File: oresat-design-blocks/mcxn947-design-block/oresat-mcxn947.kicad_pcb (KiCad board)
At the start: 2 copper layers, 1 part, among them IC1 MCXN947VKLT

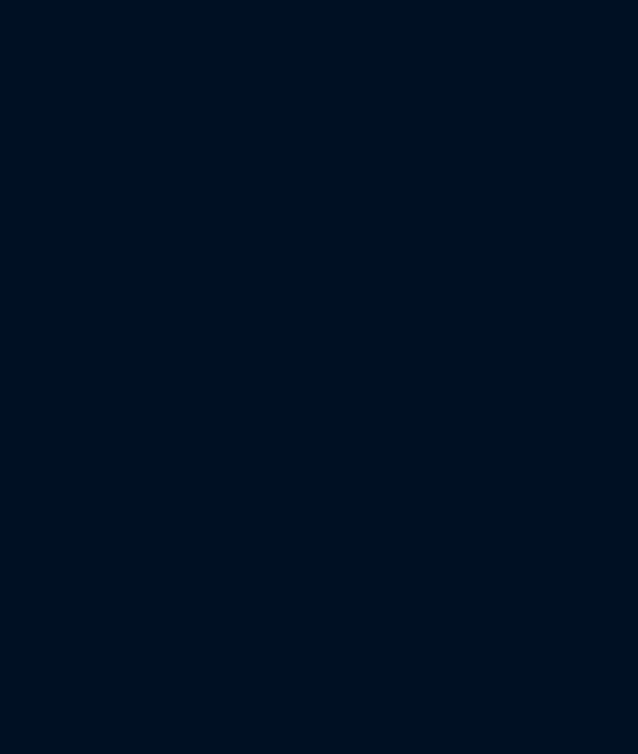
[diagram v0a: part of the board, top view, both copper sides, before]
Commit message: Removed lock file, updated .gitignore file
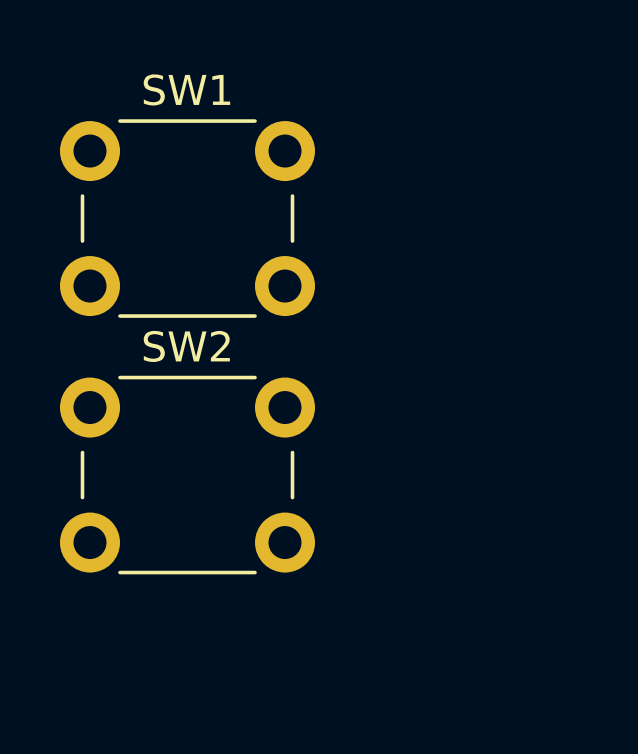
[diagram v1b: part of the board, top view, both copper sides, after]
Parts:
- added SW1: RESET, Button_Switch_THT:SW_PUSH_6mm, F.Cu at (19.9, 21.2)
- added SW2: ISP(BOOT), Button_Switch_THT:SW_PUSH_6mm, F.Cu at (19.9, 29.8)
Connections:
- IC1 pad 10: unconnected-(IC1C-P1_30-Pad10) -> Net-(IC1C-P1_30)
- IC1 pad 101: unconnected-(IC1A-EP-Pad101) -> GND
- IC1 pad 11: unconnected-(IC1C-P1_31-Pad11) -> Net-(IC1C-P1_31)
- IC1 pad 76: unconnected-(IC1B-P0_0-Pad76) -> Net-(IC1B-P0_0)
- IC1 pad 77: unconnected-(IC1B-P0_1-Pad77) -> Net-(IC1B-P0_1)
- IC1 pad 78: unconnected-(IC1B-P0_2-Pad78) -> Net-(IC1B-P0_2)
- IC1 pad 79: unconnected-(IC1B-P0_3-Pad79) -> Net-(IC1B-P0_3)
- IC1 pad 82: unconnected-(IC1B-P0_6-Pad82) -> Net-(IC1B-P0_6)
- IC1 pad 9: unconnected-(IC1A-RESET_B-Pad9) -> RESET

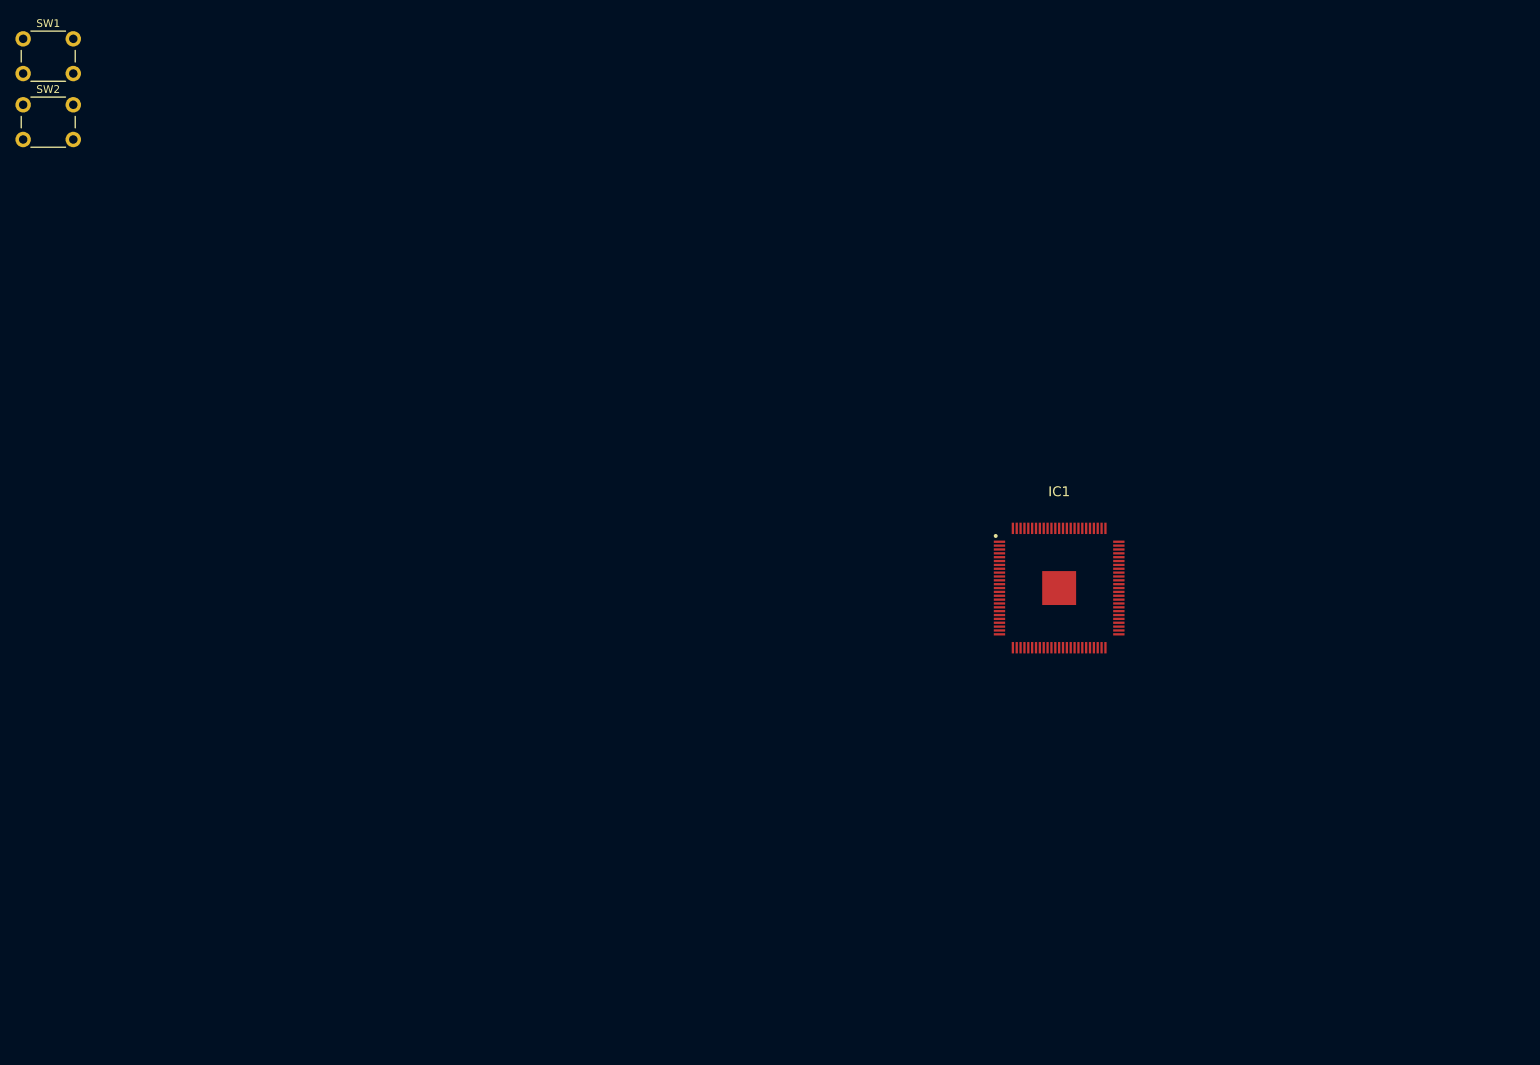
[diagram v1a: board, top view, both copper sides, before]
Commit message: Rough draft of schematic done. Power checked against eval board and reference manual. Needs one more go-over we think. Polished symbol, pin names might need another go-around with alt numbers. Added OreSat debug connector because that makes sense. Started 4 layer board layout, initial placements.
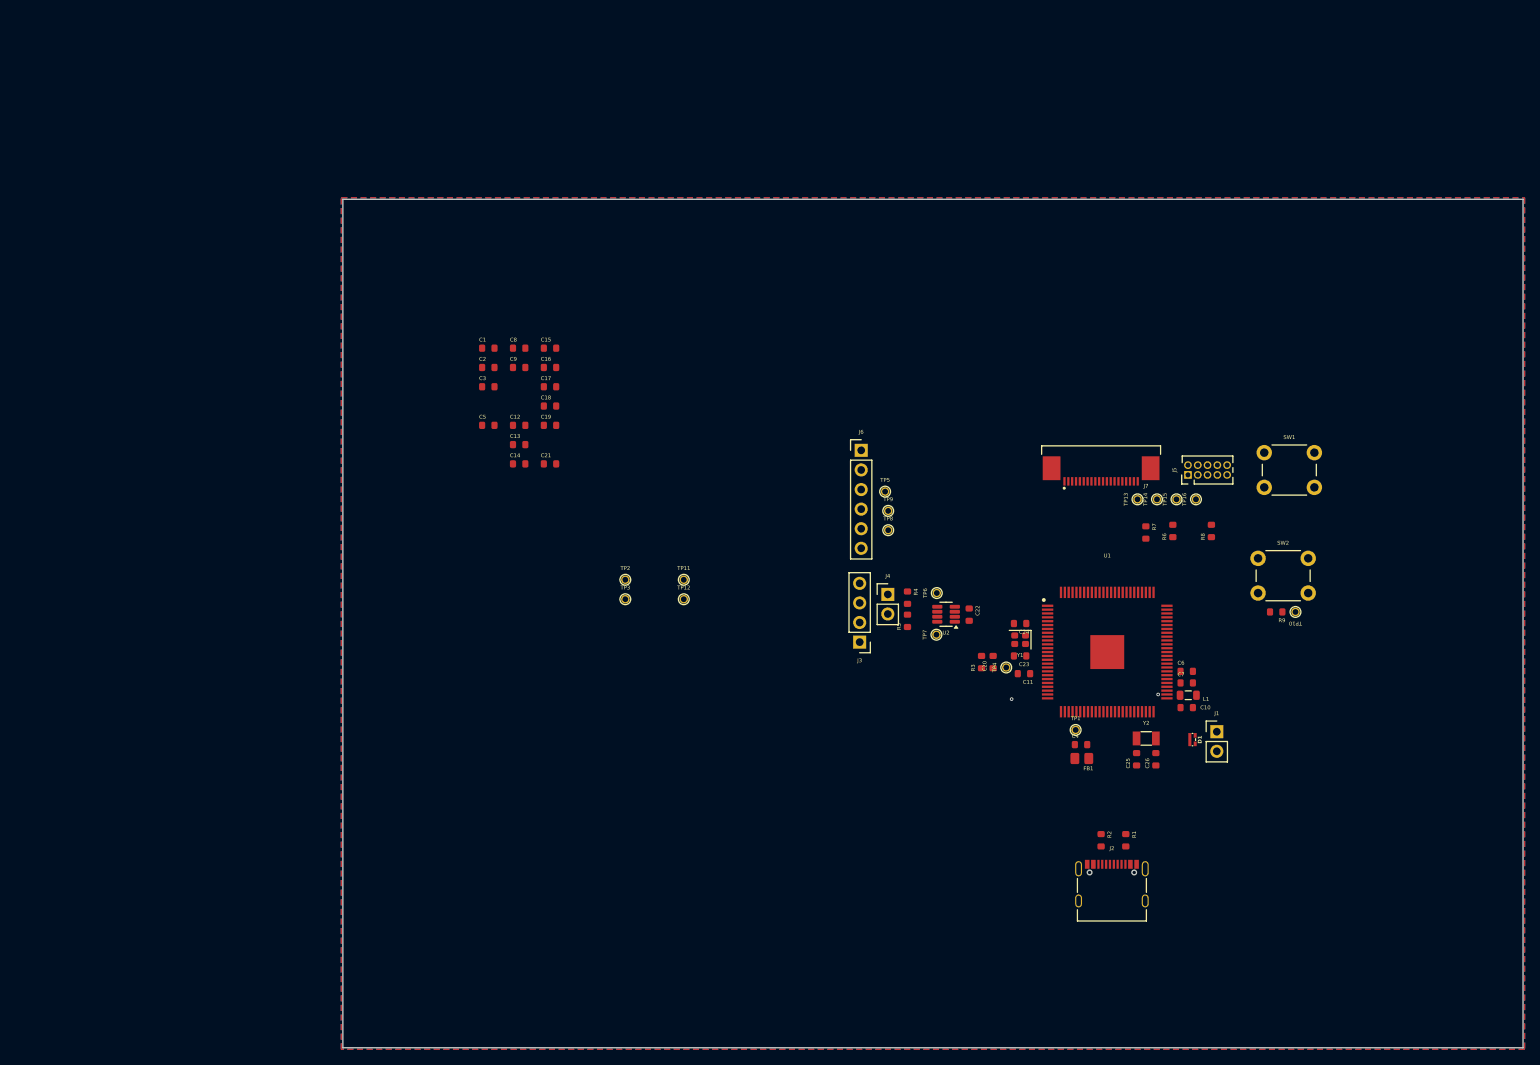
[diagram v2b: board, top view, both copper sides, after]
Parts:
- removed IC1: MCXN947VKLT, oresat-ics:MCXN947KVLT-QFP50P1600X1600X160-101N
- added C1: 100n, oresat-passives:0603-B-NOSILK, F.Cu at (80.3, 61.3)
- added C10: 6.8u, oresat-passives:0603-B-NOSILK, F.Cu at (170.8, 107.9)
- added C11: 4.7u, oresat-passives:0603-B-NOSILK, F.Cu at (149.7, 103.5)
- added C12: 100n, oresat-passives:0603-B-NOSILK, F.Cu at (84.3, 71.3)
- added C13: 100n, oresat-passives:0603-B-NOSILK, F.Cu at (84.3, 73.8)
- added C14: 100n, oresat-passives:0603-B-NOSILK, F.Cu at (84.3, 76.3)
- added C15: 100n, oresat-passives:0603-B-NOSILK, F.Cu at (88.3, 61.3)
- added C16: 100n, oresat-passives:0603-B-NOSILK, F.Cu at (88.3, 63.8)
- added C17: 100n, oresat-passives:0603-B-NOSILK, F.Cu at (88.3, 66.3)
- added C18: 100n, oresat-passives:0603-B-NOSILK, F.Cu at (88.3, 68.8)
- added C19: 100n, oresat-passives:0603-B-NOSILK, F.Cu at (88.3, 71.3)
- added C2: 100n, oresat-passives:0603-B-NOSILK, F.Cu at (80.3, 63.8)
- added C20: 100n, oresat-passives:0603-B-NOSILK, F.Cu at (145.7, 102.0)
- added C21: 100n, oresat-passives:0603-B-NOSILK, F.Cu at (88.3, 76.3)
- added C22: 100n, oresat-passives:0603-B-NOSILK, F.Cu at (142.6, 95.8)
- added C23: 4.7p, oresat-passives:0603-B-NOSILK, F.Cu at (149.2, 101.2)
- added C24: 4.7p, oresat-passives:0603-B-NOSILK, F.Cu at (149.2, 97.0)
- added C25: 4.7p, oresat-passives:0603-B-NOSILK, F.Cu at (164.3, 114.6)
- added C26: 4.7p, oresat-passives:0603-B-NOSILK, F.Cu at (166.8, 114.6)
- added C3: 100n, oresat-passives:0603-B-NOSILK, F.Cu at (80.3, 66.3)
- added C4: 1u, oresat-passives:0603-B-NOSILK, F.Cu at (157.1, 112.7)
- added C5: 100n, oresat-passives:0603-B-NOSILK, F.Cu at (80.3, 71.3)
- added C6: 2.2u, oresat-passives:0603-B-NOSILK, F.Cu at (170.8, 103.2)
- added C7: 4.7u, oresat-passives:0603-B-NOSILK, F.Cu at (170.8, 104.7)
- added C8: 100n, oresat-passives:0603-B-NOSILK, F.Cu at (84.3, 61.3)
- added C9: 100n, oresat-passives:0603-B-NOSILK, F.Cu at (84.3, 63.8)
- added D1: BAT54CW, oresat-passives:PAT0816(0603), F.Cu at (171.6, 112.0)
- added FB1: 120 ohm ?, oresat-passives:0805-B-NOSILK, F.Cu at (157.2, 114.5)
- added J1: BKUP-BATT, Connector_PinHeader_2.54mm:PinHeader_1x02_P2.54mm_Vertical, F.Cu at (174.7, 111.0)
- added J2: USB_C_Receptacle_USB2.0_14P, Connector_USB:USB_C_Receptacle_Palconn_UTC16-G, F.Cu at (161.1, 130.7)
- added J3: CAN, Connector_PinHeader_2.54mm:PinHeader_1x04_P2.54mm_Vertical, F.Cu at (128.4, 99.4)
- added J4: TERM, Connector_PinHeader_2.54mm:PinHeader_1x02_P2.54mm_Vertical, F.Cu at (132.1, 93.2)
- added J5: 10pin ARM SWD, Connector_PinHeader_1.27mm:PinHeader_2x05_P1.27mm_Vertical, F.Cu at (171.0, 77.7)
- added J6: FTDI-UART-6PIN, Connector_PinHeader_2.54mm:PinHeader_1x06_P2.54mm_Vertical, F.Cu at (128.6, 74.5)
- added J7: ~, oresat-connectors:J-TE-2-1734592-0, F.Cu at (159.7, 76.9)
- added L1: 1.5u, Inductor_SMD:L_0805_2012Metric, F.Cu at (171.0, 106.3)
- added R1: 5.11k, oresat-passives:0603-B-NOSILK, F.Cu at (162.9, 125.1)
- added R2: 5.11k, oresat-passives:0603-B-NOSILK, F.Cu at (159.7, 125.1)
- added R3: 10k, oresat-passives:0603-B-NOSILK, F.Cu at (144.2, 102.0)
- added R4: 60.4, oresat-passives:0603-B-NOSILK, F.Cu at (134.6, 93.7)
- added R5: 60.4, oresat-passives:0603-B-NOSILK, F.Cu at (134.6, 96.7)
- added R6: 10k, oresat-passives:0603-B-NOSILK, F.Cu at (169.0, 85.0)
- added R7: 10k, oresat-passives:0603-B-NOSILK, F.Cu at (165.5, 85.2)
- added R8: 10k, oresat-passives:0603-B-NOSILK, F.Cu at (174.0, 85.0)
- added R9: 10k, oresat-passives:0603-B-NOSILK, F.Cu at (182.4, 95.5)
- added TP1: Test-Point, oresat-misc:TestPoint-0.75mm-th, F.Cu at (156.4, 110.8)
- added TP10: Test-Point, oresat-misc:TestPoint-0.75mm-th, F.Cu at (184.9, 95.5)
- added TP11: Test-Point, oresat-misc:TestPoint-0.75mm-th, F.Cu at (105.6, 91.3)
- added TP12: Test-Point, oresat-misc:TestPoint-0.75mm-th, F.Cu at (105.6, 93.9)
- added TP13: Test-Point, oresat-misc:TestPoint-0.75mm-th, F.Cu at (164.4, 80.9)
- added TP14: Test-Point, oresat-misc:TestPoint-0.75mm-th, F.Cu at (166.9, 80.9)
- added TP15: Test-Point, oresat-misc:TestPoint-0.75mm-th, F.Cu at (169.5, 80.9)
- added TP16: Test-Point, oresat-misc:TestPoint-0.75mm-th, F.Cu at (172.0, 80.9)
- added TP2: Test-Point, oresat-misc:TestPoint-0.75mm-th, F.Cu at (98.0, 91.3)
- added TP3: Test-Point, oresat-misc:TestPoint-0.75mm-th, F.Cu at (98.0, 93.9)
- added TP4: Test-Point, oresat-misc:TestPoint-0.75mm-th, F.Cu at (147.4, 102.7)
- added TP5: Test-Point, oresat-misc:TestPoint-0.75mm-th, F.Cu at (131.7, 79.9)
- added TP6: Test-Point, oresat-misc:TestPoint-0.75mm-th, F.Cu at (138.4, 93.0)
- added TP7: Test-Point, oresat-misc:TestPoint-0.75mm-th, F.Cu at (138.3, 98.5)
- added TP8: Test-Point, oresat-misc:TestPoint-0.75mm-th, F.Cu at (132.1, 84.9)
- added TP9: Test-Point, oresat-misc:TestPoint-0.75mm-th, F.Cu at (132.1, 82.4)
- added U1: MCXN947VKLT, oresat-ics:MCXN947KVLT-QFP50P1600X1600X160-101N, F.Cu at (160.5, 100.7)
- added U2: TCAN330, Package_TO_SOT_SMD:SOT-23-8, F.Cu at (139.6, 95.8)
- added Y1: 24 MHz, Crystal:Crystal_SMD_2016-4Pin_2.0x1.6mm, F.Cu at (149.2, 99.1)
- added Y2: 32.768 KHz, Crystal:Crystal_SMD_3215-2Pin_3.2x1.5mm, F.Cu at (165.6, 111.9)
- moved SW2 170.6 mm to (180.1, 88.5)
- moved SW1 169.6 mm to (180.8, 74.8)
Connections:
- SW2 pad 2: Net-(IC1B-P0_6) -> /BOOT
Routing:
- net GND: vias 0 -> 2
- added copper zone on B.Cu, net GND
- added copper zone on F.Cu, net GND
- added copper zone on In1.Cu, net GND
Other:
- board outline added: 153 x 110 mm
- copper layers 2 -> 4

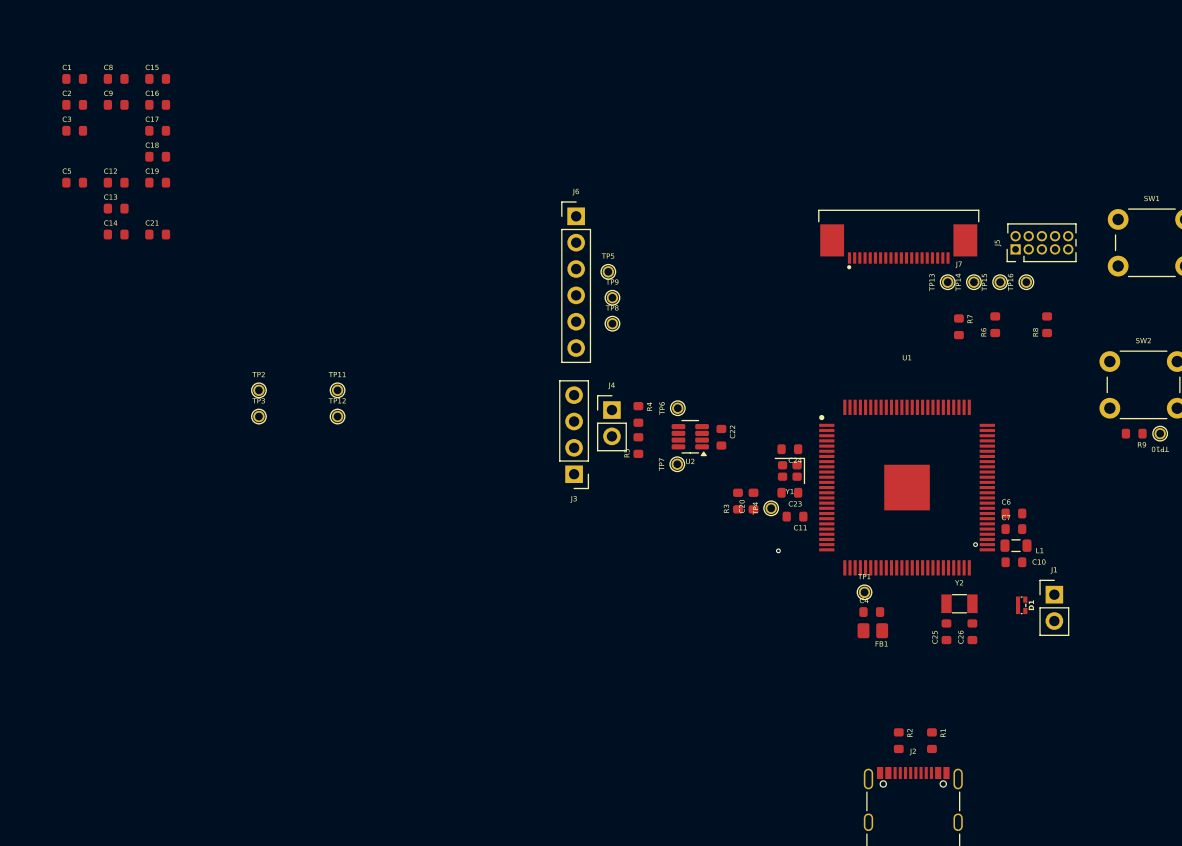
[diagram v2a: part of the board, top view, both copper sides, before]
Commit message: More preliminary layout, focusing on power.
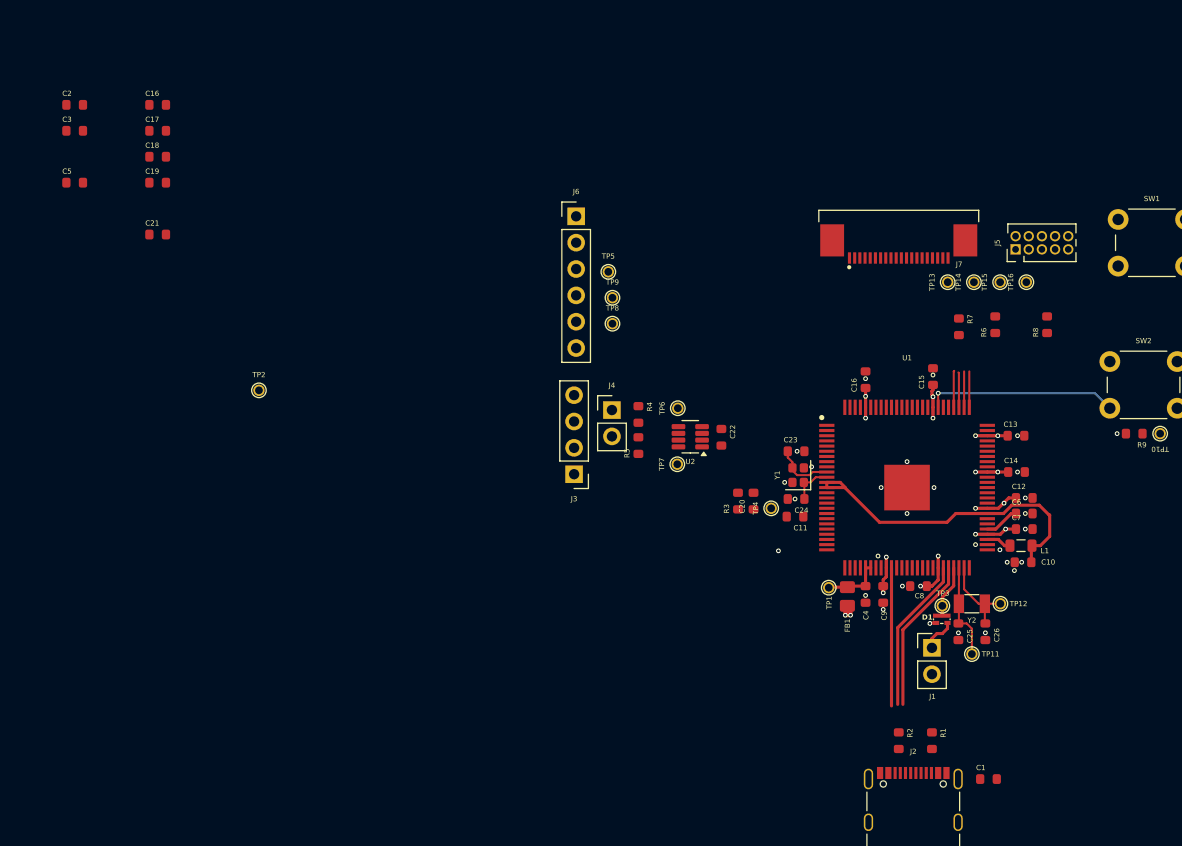
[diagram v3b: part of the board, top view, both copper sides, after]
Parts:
- added C16: 100n, oresat-passives:0603-B-NOSILK, F.Cu at (156.5, 90.3)
- moved C1 111.0 mm to (168.3, 128.8)
- moved C12 92.7 mm to (171.8, 101.7)
- moved C8 91.5 mm to (161.6, 110.2), turned to 180 degrees
- moved C14 89.8 mm to (171.1, 99.2)
- moved C13 89.5 mm to (171.0, 95.7)
- moved C9 87.7 mm to (158.2, 111.0), turned to -90 degrees
- moved C15 80.1 mm to (163.0, 90.0), turned to 90 degrees
- moved TP3 68.4 mm to (163.9, 112.1)
- moved TP12 66.4 mm to (169.5, 111.9)
- moved TP11 66.2 mm to (166.8, 116.8)
- moved J1 12.9 mm to (162.9, 116.2)
- moved D1 7.82 mm to (163.8, 113.4), turned to 180 degrees
- moved C24 4.84 mm to (149.8, 101.8)
- moved FB1 4.11 mm to (154.8, 111.2), turned to 90 degrees
- moved C23 4.04 mm to (149.8, 97.2), turned to 0 degrees
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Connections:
- Y1 pad 3: GND -> Net-(U1C-P1_30)
- Y1 pad 4: Net-(U1C-P1_30) -> GND
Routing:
- net +3.3V: track 0.00 -> 32.8 mm, vias 0 -> 20
- net VDD: track 0.00 -> 32.2 mm
- net /BOOT: track 0.00 -> 18.5 mm, vias 0 -> 1
- net USB_D-: track 0.00 -> 15.0 mm
- net USB_D+: track 0.00 -> 15.0 mm
- net VBUS: track 0.00 -> 13.3 mm
- net Net-(U1G-P5_0): track 0.00 -> 9.34 mm
- net Net-(U1G-P5_1): track 0.00 -> 8.06 mm
- net Net-(U1A-VDD_ANA): track 0.00 -> 6.09 mm
- net Net-(U1C-P1_30): track 0.00 -> 5.66 mm
- net Net-(U1A-VDD_BAT): track 0.00 -> 5.09 mm
- net Net-(U1C-P1_31): track 0.00 -> 4.04 mm
- net /SWI: track 0.00 -> 3.53 mm
- net /SWDIO: track 0.00 -> 3.46 mm
- net /SWCLK: track 0.00 -> 3.46 mm
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- added copper zone on In2.Cu, net +3.3V
